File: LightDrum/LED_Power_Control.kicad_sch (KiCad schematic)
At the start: 12 parts, among them J2 STD BARREL JACK, J3 STD BARREL JACK, K1 ALQ112, K2 ALQ112, U39 74HCT2G08, U40 SSM3K361R_SOT23F

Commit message: Add docs and gerbers for REV7
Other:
- title: RGB STRIP POWER LOCKOUT -> LightDrum
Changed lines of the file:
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@@
   (paper "A4")
   (title_block
-    (title "RGB STRIP POWER LOCKOUT")
-    (rev "REV6")
+    (title "LightDrum")
+    (rev "REV7")
     (company "Daxxn Industries")
   )

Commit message: First pass over schematic (WIP)
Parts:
- R147, R91, R94: value ${P-RES} -> 10K
- R90: value ${DCL-RES} -> 100
- U39: value 74HCT2G08 -> 74HC2G08
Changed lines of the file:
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@@
   (title_block
     (title "LightDrum")
-    (rev "REV7")
+    (rev "REV8")
     (company "Daxxn Industries")
   )
@@
       (effects (font (size 1.27 1.27)) (justify right))
     )
-    (property "Value" "${P-RES}" (id 1) (at 42.164 50.038 0)
+    (property "Value" "10K" (id 1) (at 42.164 50.038 0)
       (effects (font (size 1.27 1.27)) (justify right))
     )
@@
     (in_bom yes) (on_board yes)
     (property "Reference" "R90" (id 0) (at 96.52 60.96 90))
-    (property "Value" "${DCL-RES}" (id 1) (at 96.52 62.738 90))
+    (property "Value" "100" (id 1) (at 96.52 62.738 90))
     (property "Footprint" "Resistor_SMD:R_0805_2012Metric" (id 2) (at 96.52 64.77 0)
       (effects (font (size 1.27 1.27)) hide)
@@
       (effects (font (size 1.27 1.27)) hide)
     )
-    (property "Datasheet" "C:\\Users\\Daxxn\\Documents\\Electrical\\Datasheets\\SSM3K361R.pdf" (id 3) (at 106.68 49.53 0)
+    (property "Datasheet" "%LOCAL_DATASHEETS%\\SSM3K361R.pdf" (id 3) (at 106.68 49.53 0)
       (effects (font (size 1.27 1.27)) hide)
     )
@@
     (in_bom yes) (on_board yes)
     (property "Reference" "U39" (id 0) (at 81.28 50.292 0))
-    (property "Value" "74HCT2G08" (id 1) (at 81.28 52.07 0))
+    (property "Value" "74HC2G08" (id 1) (at 81.28 52.07 0))
     (property "Footprint" "Package_SO:TSSOP-8_3x3mm_P0.65mm" (id 2) (at 81.28 38.1 0)
       (effects (font (size 1.27 1.27)) hide)
     )
-    (property "Datasheet" "C:\\Users\\Daxxn\\Documents\\Electrical\\Datasheets\\74HC2G08.pdf" (id 3) (at 81.28 35.56 0)
+    (property "Datasheet" "%LOCAL_DATASHEETS%\\74HC2G08.pdf" (id 3) (at 81.28 35.56 0)
       (effects (font (size 1.27 1.27)) hide)
     )
@@
       (effects (font (size 1.27 1.27)) (justify right))
     )
-    (property "Value" "${P-RES}" (id 1) (at 99.06 69.596 0)
+    (property "Value" "10K" (id 1) (at 99.06 69.596 0)
       (effects (font (size 1.27 1.27)) (justify right))
     )
@@
     (in_bom yes) (on_board yes)
     (property "Reference" "U39" (id 0) (at 62.23 47.752 0))
-    (property "Value" "74HCT2G08" (id 1) (at 62.23 49.53 0))
+    (property "Value" "74HC2G08" (id 1) (at 62.23 49.53 0))
     (property "Footprint" "Package_SO:TSSOP-8_3x3mm_P0.65mm" (id 2) (at 62.23 35.56 0)
       (effects (font (size 1.27 1.27)) hide)
     )
-    (property "Datasheet" "C:\\Users\\Daxxn\\Documents\\Electrical\\Datasheets\\74HC2G08.pdf" (id 3) (at 62.23 33.02 0)
+    (property "Datasheet" "%LOCAL_DATASHEETS%\\74HC2G08.pdf" (id 3) (at 62.23 33.02 0)
       (effects (font (size 1.27 1.27)) hide)
     )
@@
       (effects (font (size 1.27 1.27)) (justify right))
     )
-    (property "Value" "${P-RES}" (id 1) (at 46.736 50.038 0)
-      (effects (font (size 1.27 1.27)) (justify right))
-    )
+    (property "Value" "10K" (id 1) (at 46.736 50.038 0)
+      (effects (font (size 1.27 1.27)) (justify right))
+    )

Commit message: General component placement
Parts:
- D901: renamed from D7; footprint Diode_SMD:D_SMB_Handsoldering -> Diode_SMD:D_SOD-323_HandSoldering
- K901: renamed from K1; PartNumber (none) -> 1001-0001
- K902: renamed from K2; PartNumber (none) -> 1001-0001
- U901: renamed from U39; PartNumber (none) -> 0802-0005
- U902: renamed from U40; PartNumber (none) -> 0703-0002
- renumbered F1 to F901, J2 to J901, J3 to J902, R94 to R901, R147 to R902, R90 to R903, R91 to R904
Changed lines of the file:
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@@
   (symbol (lib_id "Device:R_Small_US") (at 43.18 49.53 0) (unit 1)
     (in_bom yes) (on_board yes)
-    (property "Reference" "R94" (id 0) (at 42.164 48.26 0)
+    (property "Reference" "R901" (id 0) (at 42.164 48.26 0)
       (effects (font (size 1.27 1.27)) (justify right))
     )
@@
   (symbol (lib_id "Connector:Barrel_Jack_Switch") (at 25.4 39.37 0) (unit 1)
     (in_bom yes) (on_board yes)
-    (property "Reference" "J2" (id 0) (at 20.32 32.512 0)
+    (property "Reference" "J901" (id 0) (at 20.32 32.512 0)
       (effects (font (size 1.27 1.27)) (justify left))
     )
@@
   (symbol (lib_id "power:+12V") (at 147.32 35.56 0) (unit 1)
     (in_bom yes) (on_board yes)
-    (property "Reference" "#PWR058" (id 0) (at 147.32 39.37 0)
+    (property "Reference" "#PWR0901" (id 0) (at 147.32 39.37 0)
       (effects (font (size 1.27 1.27)) hide)
     )
@@
   (symbol (lib_id "Device:R_Small_US") (at 96.52 64.77 90) (unit 1)
     (in_bom yes) (on_board yes)
-    (property "Reference" "R90" (id 0) (at 96.52 60.96 90))
+    (property "Reference" "R903" (id 0) (at 96.52 60.96 90))
     (property "Value" "100" (id 1) (at 96.52 62.738 90))
     (property "Footprint" "Resistor_SMD:R_0805_2012Metric" (id 2) (at 96.52 64.77 0)
@@
   (symbol (lib_id "Daxxn_Transistors:SSM3K361R_SOT23F") (at 105.41 64.77 0) (unit 1)
     (in_bom yes) (on_board yes)
-    (property "Reference" "U40" (id 0) (at 107.95 64.008 0)
+    (property "Reference" "U902" (id 0) (at 107.95 64.008 0)
       (effects (font (size 1.27 1.27)) (justify left))
     )
@@
       (effects (font (size 1.27 1.27)) hide)
     )
+    (property "PartNumber" "0703-0002" (id 4) (at 96.52 57.15 0))
     (pin "1")
     (pin "2")
@@
   (symbol (lib_id "power:GND") (at 34.29 57.15 0) (unit 1)
     (in_bom yes) (on_board yes)
-    (property "Reference" "#PWR053" (id 0) (at 34.29 63.5 0)
+    (property "Reference" "#PWR0905" (id 0) (at 34.29 63.5 0)
       (effects (font (size 1.27 1.27)) hide)
     )
@@
   (symbol (lib_id "power:Vdrive") (at 127 53.34 0) (unit 1)
     (in_bom yes) (on_board yes)
-    (property "Reference" "#PWR057" (id 0) (at 121.92 57.15 0)
+    (property "Reference" "#PWR0903" (id 0) (at 121.92 57.15 0)
       (effects (font (size 1.27 1.27)) hide)
     )
@@
   (symbol (lib_id "Daxxn_Logic:74HCT2G08") (at 81.28 58.42 0) (unit 2)
     (in_bom yes) (on_board yes)
-    (property "Reference" "U39" (id 0) (at 81.28 50.292 0))
+    (property "Reference" "U901" (id 0) (at 81.28 50.292 0))
     (property "Value" "74HC2G08" (id 1) (at 81.28 52.07 0))
     (property "Footprint" "Package_SO:TSSOP-8_3x3mm_P0.65mm" (id 2) (at 81.28 38.1 0)
@@
     (property "Datasheet" "%LOCAL_DATASHEETS%\\74HC2G08.pdf" (id 3) (at 81.28 35.56 0)
       (effects (font (size 1.27 1.27)) hide)
+    )
+    (property "PartNumber" "0802-0005" (id 4) (at 71.12 57.15 0)
+      (effects (font (size 1.27 1.27)) (justify right))
     )
     (pin "1")
@@
   (symbol (lib_id "power:GND") (at 106.68 73.66 0) (unit 1)
     (in_bom yes) (on_board yes)
-    (property "Reference" "#PWR056" (id 0) (at 106.68 80.01 0)
+    (property "Reference" "#PWR0906" (id 0) (at 106.68 80.01 0)
       (effects (font (size 1.27 1.27)) hide)
     )
@@
   (symbol (lib_id "Device:Fuse_Small") (at 91.44 36.83 0) (unit 1)
     (in_bom yes) (on_board yes)
-    (property "Reference" "F1" (id 0) (at 91.44 33.528 0))
+    (property "Reference" "F901" (id 0) (at 91.44 33.528 0))
     (property "Value" "10A" (id 1) (at 91.44 35.306 0))
     (property "Footprint" "Daxxn_Protection:3557-10" (id 2) (at 91.44 36.83 0)
@@
   (symbol (lib_id "Connector:Barrel_Jack_Switch") (at 25.4 53.34 0) (unit 1)
     (in_bom yes) (on_board yes)
-    (property "Reference" "J3" (id 0) (at 20.32 46.482 0)
+    (property "Reference" "J902" (id 0) (at 20.32 46.482 0)
       (effects (font (size 1.27 1.27)) (justify left))
     )
@@
   (symbol (lib_id "power:VCC") (at 44.45 44.45 0) (unit 1)
     (in_bom yes) (on_board yes)
-    (property "Reference" "#PWR0122" (id 0) (at 44.45 48.26 0)
+    (property "Reference" "#PWR0902" (id 0) (at 44.45 48.26 0)
       (effects (font (size 1.27 1.27)) hide)
     )
@@
   (symbol (lib_id "power:Vdrive") (at 157.48 53.34 0) (unit 1)
     (in_bom yes) (on_board yes)
-    (property "Reference" "#PWR059" (id 0) (at 152.4 57.15 0)
+    (property "Reference" "#PWR0904" (id 0) (at 152.4 57.15 0)
       (effects (font (size 1.27 1.27)) hide)
     )
@@
   (symbol (lib_id "Device:R_Small_US") (at 100.33 68.58 0) (unit 1)
     (in_bom yes) (on_board yes)
-    (property "Reference" "R91" (id 0) (at 99.06 67.818 0)
+    (property "Reference" "R904" (id 0) (at 99.06 67.818 0)
       (effects (font (size 1.27 1.27)) (justify right))
     )
@@
     (pin "2")
   )
-  (symbol (lib_id "Daxxn_Logic:74HCT2G08") (at 62.23 55.88 0) (unit 1)
-    (in_bom yes) (on_board yes)
-    (property "Reference" "U39" (id 0) (at 62.23 47.752 0))
+  (symbol (lib_name "74HCT2G08_1") (lib_id "Daxxn_Logic:74HCT2G08") (at 62.23 55.88 0) (unit 1)
+    (in_bom yes) (on_board yes)
+    (property "Reference" "U901" (id 0) (at 62.23 47.752 0))
     (property "Value" "74HC2G08" (id 1) (at 62.23 49.53 0))
     (property "Footprint" "Package_SO:TSSOP-8_3x3mm_P0.65mm" (id 2) (at 62.23 35.56 0)
@@
     (property "Datasheet" "%LOCAL_DATASHEETS%\\74HC2G08.pdf" (id 3) (at 62.23 33.02 0)
       (effects (font (size 1.27 1.27)) hide)
+    )
+    (property "PartNumber" "0802-0005" (id 4) (at 52.07 54.61 0)
+      (effects (font (size 1.27 1.27)) (justify right))
     )
     (pin "1")
@@
   (symbol (lib_id "Device:D_Schottky") (at 96.52 45.72 270) (unit 1)
     (in_bom yes) (on_board yes)
-    (property "Reference" "D7" (id 0) (at 94.996 44.704 90)
+    (property "Reference" "D901" (id 0) (at 94.996 44.704 90)
       (effects (font (size 1.27 1.27)) (justify right))
     )
@@
       (effects (font (size 1.27 1.27)) (justify right))
     )
-    (property "Footprint" "Diode_SMD:D_SMB_Handsoldering" (id 2) (at 96.52 45.72 0)
+    (property "Footprint" "Diode_SMD:D_SOD-323_HandSoldering" (id 2) (at 96.52 45.72 0)
       (effects (font (size 1.27 1.27)) hide)
     )
@@
   (symbol (lib_id "Daxxn_Relays:ALQ112") (at 111.76 45.72 0) (mirror x) (unit 1)
     (in_bom yes) (on_board yes)
-    (property "Reference" "K1" (id 0) (at 122.174 41.402 0)
+    (property "Reference" "K901" (id 0) (at 122.174 41.402 0)
       (effects (font (size 1.27 1.27)) (justify left))
     )
@@
     (property "Datasheet" "http://www.omron.com/ecb/products/pdf/en-g5le.pdf" (id 3) (at 111.76 62.23 0)
       (effects (font (size 1.27 1.27)) hide)
+    )
+    (property "PartNumber" "1001-0001" (id 4) (at 123.19 44.45 0)
+      (effects (font (size 1.27 1.27)) (justify left))
     )
     (pin "1")
@@
   (symbol (lib_id "Device:R_Small_US") (at 45.72 49.53 180) (unit 1)
     (in_bom yes) (on_board yes)
-    (property "Reference" "R147" (id 0) (at 46.736 48.26 0)
+    (property "Reference" "R902" (id 0) (at 46.736 48.26 0)
       (effects (font (size 1.27 1.27)) (justify right))
     )
@@
     (pin "2")
   )
-  (symbol (lib_id "Daxxn_Relays:ALQ112") (at 142.24 45.72 0) (mirror x) (unit 1)
-    (in_bom yes) (on_board yes)
-    (property "Reference" "K2" (id 0) (at 152.654 41.402 0)
+  (symbol (lib_name "ALQ112_1") (lib_id "Daxxn_Relays:ALQ112") (at 142.24 45.72 0) (mirror x) (unit 1)
+    (in_bom yes) (on_board yes)
+    (property "Reference" "K902" (id 0) (at 152.654 41.402 0)
       (effects (font (size 1.27 1.27)) (justify left))
     )
@@
       (effects (font (size 1.27 1.27)) hide)
     )
-    (pin "1")
+    (property "PartNumber" "1001-0001" (id 4) (at 153.67 44.45 0)
+      (effects (font (size 1.27 1.27)) (justify left))
+    )
+    (pin "1")

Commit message: Simplify analog power supply and add some routing
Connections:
- net VCC renamed VDD
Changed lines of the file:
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@@
     (pin "8")
+  )
+  (symbol (lib_id "power:VDD") (at 44.45 44.45 0) (unit 1)
+    (in_bom yes) (on_board yes)
+    (property "Reference" "#PWR0120" (id 0) (at 44.45 48.26 0)
+      (effects (font (size 1.27 1.27)) hide)
+    )
+    (property "Value" "VDD" (id 1) (at 44.45 40.64 0))
+    (property "Footprint" "" (id 2) (at 44.45 44.45 0)
+      (effects (font (size 1.27 1.27)) hide)
+    )
+    (property "Datasheet" "" (id 3) (at 44.45 44.45 0)
+      (effects (font (size 1.27 1.27)) hide)
+    )
+    (pin "1")
   )
   (symbol (lib_id "power:GND") (at 106.68 73.66 0) (unit 1)
@@
     (pin "3")
   )
-  (symbol (lib_id "power:VCC") (at 44.45 44.45 0) (unit 1)
-    (in_bom yes) (on_board yes)
-    (property "Reference" "#PWR0902" (id 0) (at 44.45 48.26 0)
-      (effects (font (size 1.27 1.27)) hide)
-    )
-    (property "Value" "VCC" (id 1) (at 44.45 40.64 0))
-    (property "Footprint" "" (id 2) (at 44.45 44.45 0)
-      (effects (font (size 1.27 1.27)) hide)
-    )
-    (property "Datasheet" "" (id 3) (at 44.45 44.45 0)
-      (effects (font (size 1.27 1.27)) hide)
-    )
-    (pin "1")
-  )
   (symbol (lib_id "power:Vdrive") (at 157.48 53.34 0) (unit 1)

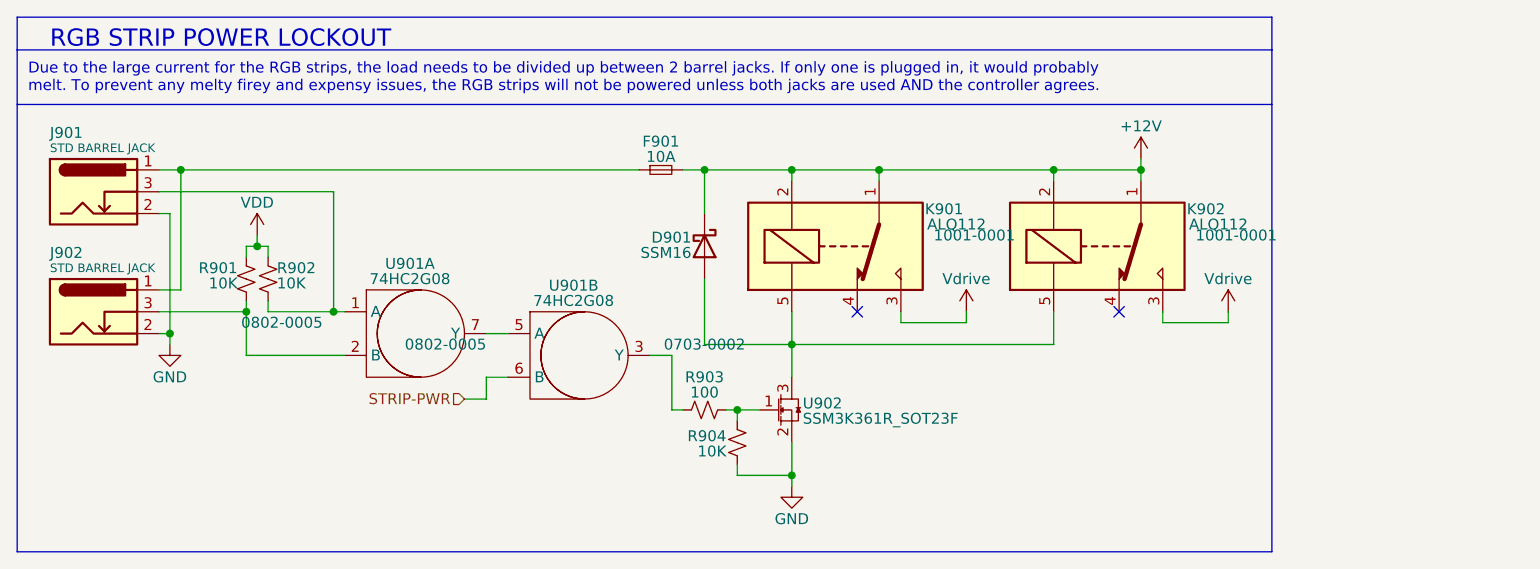
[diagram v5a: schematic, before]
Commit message: Replace barrel jacks with proper DIN4 conn and more
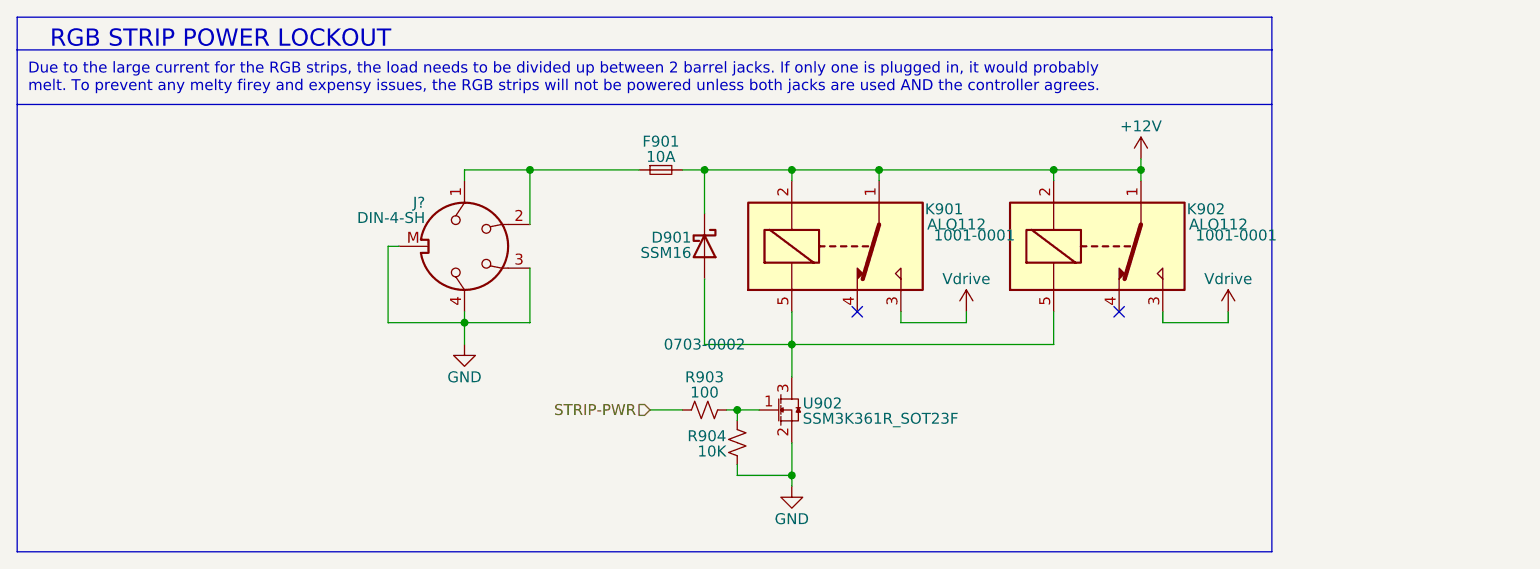
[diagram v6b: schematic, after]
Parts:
- removed J901, J902: STD BARREL JACK, Daxxn_Connectors:BarrelJack_Horizontal, symbol Connector:Barrel_Jack_Switch
- removed R901, R902: 10K, Resistor_SMD:R_0805_2012Metric, symbol Device:R_Small_US
- removed U901: 74HC2G08, Package_SO:TSSOP-8_3x3mm_P0.65mm, symbol Daxxn_Logic:74HCT2G08
- added J?: DIN-4-SH, Daxxn_Connectors:KPJXHT-4S-S, symbol Daxxn_Connectors:DIN-4-SH
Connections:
- net GND: now also J?.3, J?.4, J?.M
- net STRIP-PWR: now also R903.1
- net at F901.1: now also J?.1, J?.2

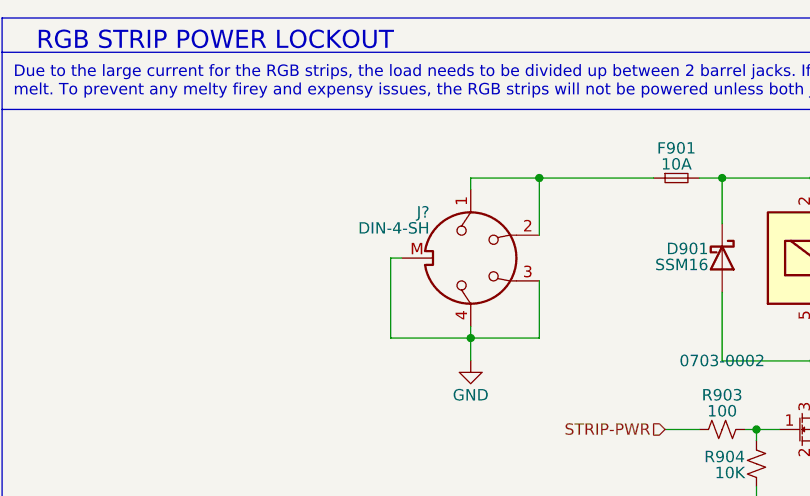
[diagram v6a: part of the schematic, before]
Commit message: Replace old MOSFETs with a more compact package
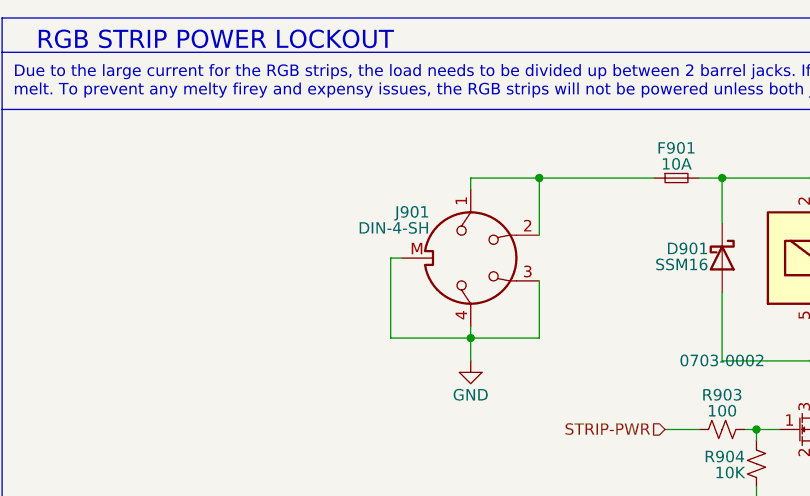
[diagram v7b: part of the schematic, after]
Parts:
- gave numbers to parts that had none: 1
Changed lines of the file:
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@@
   (symbol (lib_id "Daxxn_Connectors:DIN-4-SH") (at 68.58 45.72 270) (unit 1)
     (in_bom yes) (on_board yes)
-    (property "Reference" "J?" (id 0) (at 64.008 40.64 90)
+    (property "Reference" "J901" (id 0) (at 64.008 40.64 90)
       (effects (font (size 1.27 1.27)) (justify right))
     )
